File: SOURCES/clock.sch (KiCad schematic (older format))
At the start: 0 parts

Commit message: added clock + extended lib
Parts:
- added C?: 10u, symbol C
- added C?: 100n, symbol C
- added FB?: 330, symbol FILTER
- added U?: 5PB1006CMG, symbol 5PB1006CMG
- added X?: Crystal_Oszillator, symbol Crystal_Oszillator
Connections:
- new net: C?.1, C?.1, FB?.2, U?.12 (VDD), U?.3 (VDD), U?.8 (VDD), X?.1 (Control), X?.4 (Vcc)
- new net: U?.15 (CLKIN), X?.3 (Output)
- new net +3V3: FB?.1
- new net GND: C?.2, C?.2, U?.10 (GND), U?.2 (GND), U?.5 (GND), X?.2 (GND)
- new net MCLK0: U?.1 (Y0)
- new net MCLK1: U?.14 (Y1)
- new net MCLK2: U?.11 (Y2)
- new net MCLK3: U?.13 (Y3)
- new net MCLK4: U?.4 (Y4)
- new net MCLK5: U?.9 (Y5)
- no-connect marks 0 -> 3
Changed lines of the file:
@@
 LIBS:symbols-CS8422-CNZ
 LIBS:symbols_CS8406-CZZ
+LIBS:smd_aio-lib
+LIBS:fdsp_device_new
+LIBS:fdsp_digital_new
+LIBS:fdsp_linear_new
+LIBS:fdsp_oscillator_new
+LIBS:fdsp_transistor_new
 LIBS:smd_aio-cache
 EELAYER 25 0
@@
 $Descr A4 11693 8268
 encoding utf-8
-Sheet 1 7
+Sheet 7 7
 Title ""
 Date ""
@@
 Comment4 ""
 $EndDescr
+$Comp
+L Crystal_Oszillator X?
+U 1 1 5B071476
+P 4510 3290
+F 0 "X?" H 4510 3740 60  0000 C CNN
+F 1 "Crystal_Oszillator" H 4510 2840 60  0000 C CNN
+F 2 "" H 4410 3190 60  0000 C CNN
+F 3 "" H 4410 3190 60  0000 C CNN
+	1    4510 3290
+	1    0    0    -1
+$EndComp
+$Comp
+L FILTER FB?
+U 1 1 5B0715ED
+P 3050 2560
+F 0 "FB?" H 3050 2710 50  0000 C CNN
+F 1 "330" H 3050 2460 50  0000 C CNN
+F 2 "" H 3050 2560 50  0000 C CNN
+F 3 "" H 3050 2560 50  0000 C CNN
+	1    3050 2560
+	0    1    1    0
+$EndComp
+$Comp
+L +3V3 #PWR?
+U 1 1 5B071680
+P 3050 1930
+F 0 "#PWR?" H 3050 1780 50  0001 C CNN
+F 1 "+3V3" H 3050 2070 50  0000 C CNN
+F 2 "" H 3050 1930 60  0000 C CNN
+F 3 "" H 3050 1930 60  0000 C CNN
+	1    3050 1930
+	1    0    0    -1
+$EndComp
+$Comp
+L C C?
+U 1 1 5B0716DF
+P 3050 3270
+F 0 "C?" H 3075 3370 50  0000 L CNN
+F 1 "10u" H 3075 3170 50  0000 L CNN
+F 2 "" H 3088 3120 30  0000 C CNN
+F 3 "" H 3050 3270 60  0000 C CNN
+	1    3050 3270
+	1    0    0    -1
+$EndComp
+$Comp
+L GND #PWR?
+U 1 1 5B071722
+P 3050 3850
+F 0 "#PWR?" H 3050 3600 50  0001 C CNN
+F 1 "GND" H 3050 3700 50  0000 C CNN
+F 2 "" H 3050 3850 60  0000 C CNN
+F 3 "" H 3050 3850 60  0000 C CNN
+	1    3050 3850
+	1    0    0    -1
+$EndComp
+$Comp
+L 5PB1006CMG U?
+U 1 1 5B072592
+P 6950 3730
+F 0 "U?" H 7000 5030 60  0000 C CNN
+F 1 "5PB1006CMG" H 7100 4330 60  0000 C CNN
+F 2 "" H 6950 3730 60  0001 C CNN
+F 3 "" H 6950 3730 60  0001 C CNN
+	1    6950 3730
+	1    0    0    -1
+$EndComp
+Text GLabel 6090 2730 0    60   Output ~ 0
+MCLK0
+Text GLabel 7150 2170 1    60   Output ~ 0
+MCLK1
+Text GLabel 7400 2170 1    60   Output ~ 0
+MCLK3
+Text GLabel 8010 2980 2    60   Output ~ 0
+MCLK2
+Text GLabel 8020 3480 2    60   Output ~ 0
+MCLK5
+NoConn ~ 6650 2280
+$Comp
+L C C?
+U 1 1 5B07311B
+P 5250 3800
+F 0 "C?" H 5275 3900 50  0000 L CNN
+F 1 "100n" H 5275 3700 50  0000 L CNN
+F 2 "" H 5288 3650 30  0000 C CNN
+F 3 "" H 5250 3800 60  0000 C CNN
+	1    5250 3800
+	1    0    0    -1
+$EndComp
+$Comp
+L GND #PWR?
+U 1 1 5B0732C4
+P 5520 4790
+F 0 "#PWR?" H 5520 4540 50  0001 C CNN
+F 1 "GND" H 5520 4640 50  0000 C CNN
+F 2 "" H 5520 4790 60  0000 C CNN
+F 3 "" H 5520 4790 60  0000 C CNN
+	1    5520 4790
+	1    0    0    -1
+$EndComp
+Text GLabel 6100 3480 0    60   Output ~ 0
+MCLK4
+Wire Wire Line
+	5520 2980 6150 2980
+Wire Wire Line
+	6100 3480 6150 3480
+Connection ~ 5250 2730
+Wire Wire Line
+	5250 3650 5250 2730
+Wire Wire Line
+	5440 3540 5060 3540
+Connection ~ 7400 4230
+Wire Wire Line
+	8620 2730 7900 2730
+Wire Wire Line
+	8620 4230 8620 2730
+Connection ~ 5690 3230
+Wire Wire Line
+	7400 4230 7400 3980
+Wire Wire Line
+	5690 4230 8620 4230
+Wire Wire Line
+	5690 3230 6150 3230
+Wire Wire Line
+	5690 2730 5690 4230
+Wire Wire Line
+	3960 2730 5690 2730
+Wire Wire Line
+	5440 2030 6900 2030
+Wire Wire Line
+	6900 2030 6900 2280
+Wire Wire Line
+	7900 3480 8020 3480
+Wire Wire Line
+	7900 2980 8010 2980
+Wire Wire Line
+	7400 2170 7400 2280
+Wire Wire Line
+	7150 2170 7150 2280
+Wire Wire Line
+	6090 2730 6150 2730
+Wire Wire Line
+	5440 2030 5440 3540
+Connection ~ 5060 2730
+Wire Wire Line
+	5060 3040 5060 2730
+Connection ~ 3960 2940
+Connection ~ 3050 3540
+Wire Wire Line
+	3960 3540 3050 3540
+Connection ~ 3050 2940
+Wire Wire Line
+	3960 2730 3960 3040
+Wire Wire Line
+	3050 2940 3960 2940
+Wire Wire Line
+	3050 3420 3050 3850
+Wire Wire Line
+	3050 2910 3050 3120
+Wire Wire Line
+	3050 1930 3050 2210
+Wire Wire Line
+	5520 2980 5520 4790
+Wire Wire Line
+	5250 3950 5250 4490
+Wire Wire Line
+	5250 4490 8840 4490
+Connection ~ 5520 4490
+Wire Wire Line
+	6650 4490 6650 3980
+Wire Wire Line
+	8840 4490 8840 3230
+Wire Wire Line
+	8840 3230 7900 3230
+Connection ~ 6650 4490
+NoConn ~ 6900 3980
+NoConn ~ 7150 3980
 $EndSCHEMATC

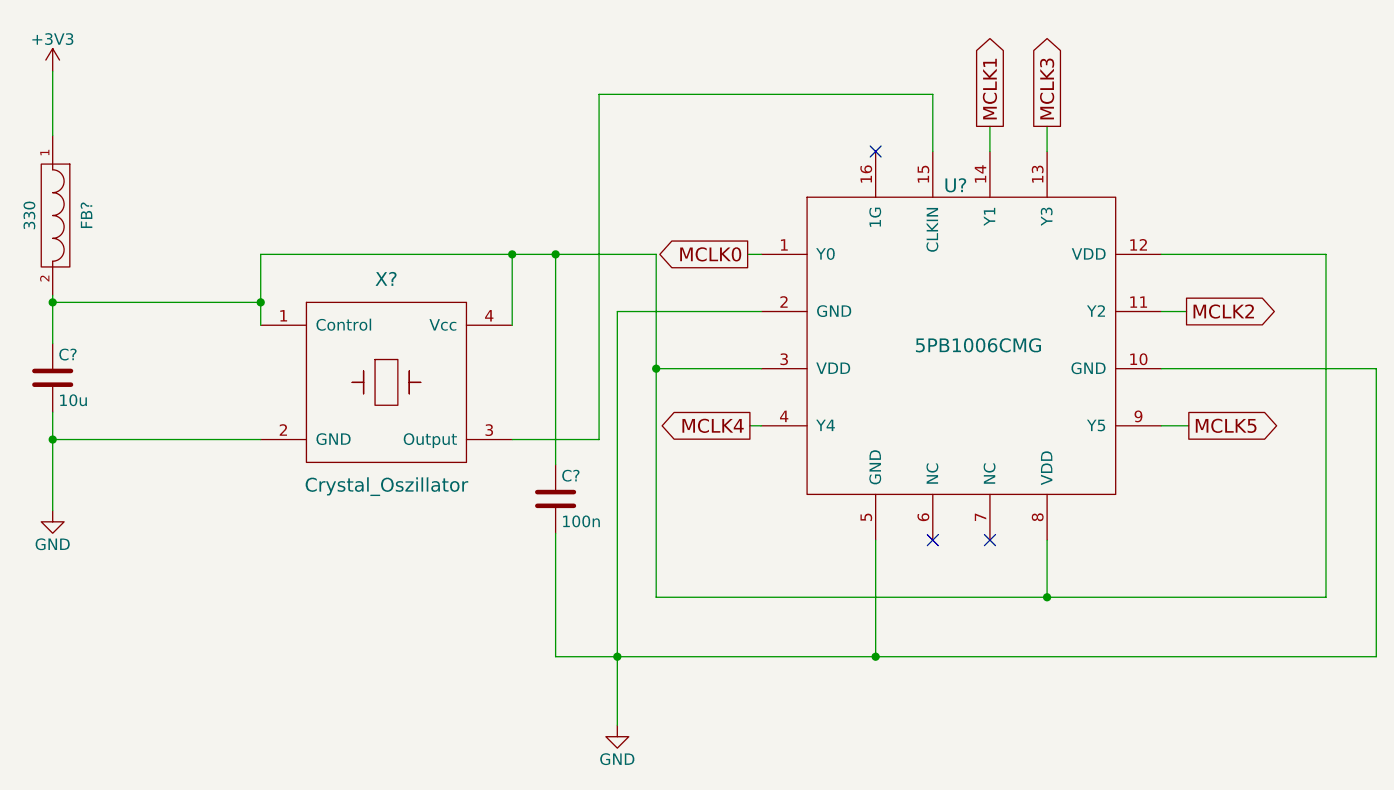
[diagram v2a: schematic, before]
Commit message: added clock
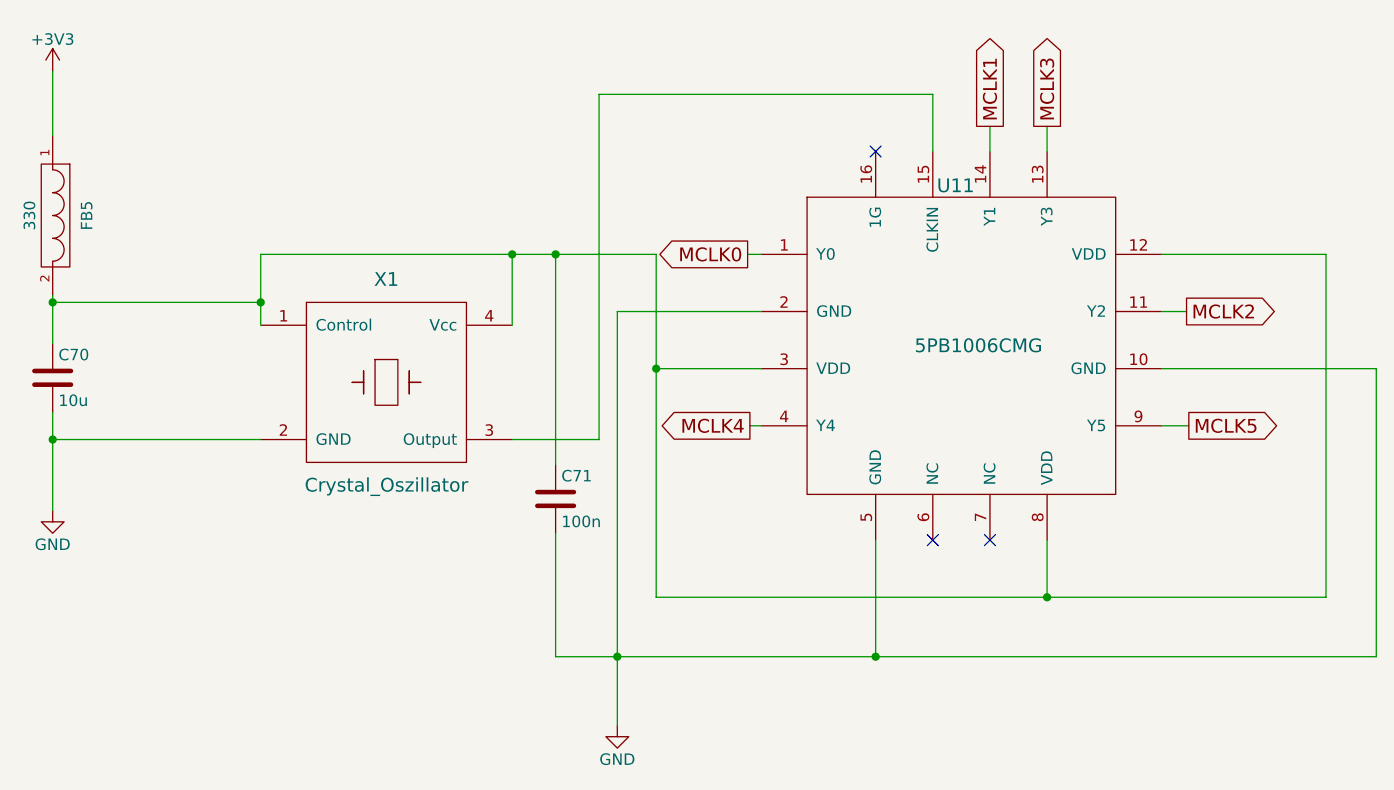
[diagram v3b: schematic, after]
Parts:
- gave numbers to parts that had none: 5
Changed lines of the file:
@@
 $EndDescr
 $Comp
-L Crystal_Oszillator X?
+L Crystal_Oszillator X1
 U 1 1 5B071476
 P 4510 3290
-F 0 "X?" H 4510 3740 60  0000 C CNN
+F 0 "X1" H 4510 3740 60  0000 C CNN
 F 1 "Crystal_Oszillator" H 4510 2840 60  0000 C CNN
 F 2 "" H 4410 3190 60  0000 C CNN
@@
 $EndComp
 $Comp
-L FILTER FB?
+L FILTER FB5
 U 1 1 5B0715ED
 P 3050 2560
-F 0 "FB?" H 3050 2710 50  0000 C CNN
+F 0 "FB5" H 3050 2710 50  0000 C CNN
 F 1 "330" H 3050 2460 50  0000 C CNN
 F 2 "" H 3050 2560 50  0000 C CNN
@@
 $EndComp
 $Comp
-L +3V3 #PWR?
+L +3V3 #PWR109
 U 1 1 5B071680
 P 3050 1930
-F 0 "#PWR?" H 3050 1780 50  0001 C CNN
+F 0 "#PWR109" H 3050 1780 50  0001 C CNN
 F 1 "+3V3" H 3050 2070 50  0000 C CNN
 F 2 "" H 3050 1930 60  0000 C CNN
@@
 $EndComp
 $Comp
-L C C?
+L C C70
 U 1 1 5B0716DF
 P 3050 3270
-F 0 "C?" H 3075 3370 50  0000 L CNN
+F 0 "C70" H 3075 3370 50  0000 L CNN
 F 1 "10u" H 3075 3170 50  0000 L CNN
 F 2 "" H 3088 3120 30  0000 C CNN
@@
 $EndComp
 $Comp
-L GND #PWR?
+L GND #PWR110
 U 1 1 5B071722
 P 3050 3850
-F 0 "#PWR?" H 3050 3600 50  0001 C CNN
+F 0 "#PWR110" H 3050 3600 50  0001 C CNN
 F 1 "GND" H 3050 3700 50  0000 C CNN
 F 2 "" H 3050 3850 60  0000 C CNN
@@
 $EndComp
 $Comp
-L 5PB1006CMG U?
+L 5PB1006CMG U11
 U 1 1 5B072592
 P 6950 3730
-F 0 "U?" H 7000 5030 60  0000 C CNN
+F 0 "U11" H 7000 5030 60  0000 C CNN
 F 1 "5PB1006CMG" H 7100 4330 60  0000 C CNN
 F 2 "" H 6950 3730 60  0001 C CNN
@@
 NoConn ~ 6650 2280
 $Comp
-L C C?
+L C C71
 U 1 1 5B07311B
 P 5250 3800
-F 0 "C?" H 5275 3900 50  0000 L CNN
+F 0 "C71" H 5275 3900 50  0000 L CNN
 F 1 "100n" H 5275 3700 50  0000 L CNN
 F 2 "" H 5288 3650 30  0000 C CNN
@@
 $EndComp
 $Comp
-L GND #PWR?
+L GND #PWR111
 U 1 1 5B0732C4
 P 5520 4790
-F 0 "#PWR?" H 5520 4540 50  0001 C CNN
+F 0 "#PWR111" H 5520 4540 50  0001 C CNN
 F 1 "GND" H 5520 4640 50  0000 C CNN
 F 2 "" H 5520 4790 60  0000 C CNN

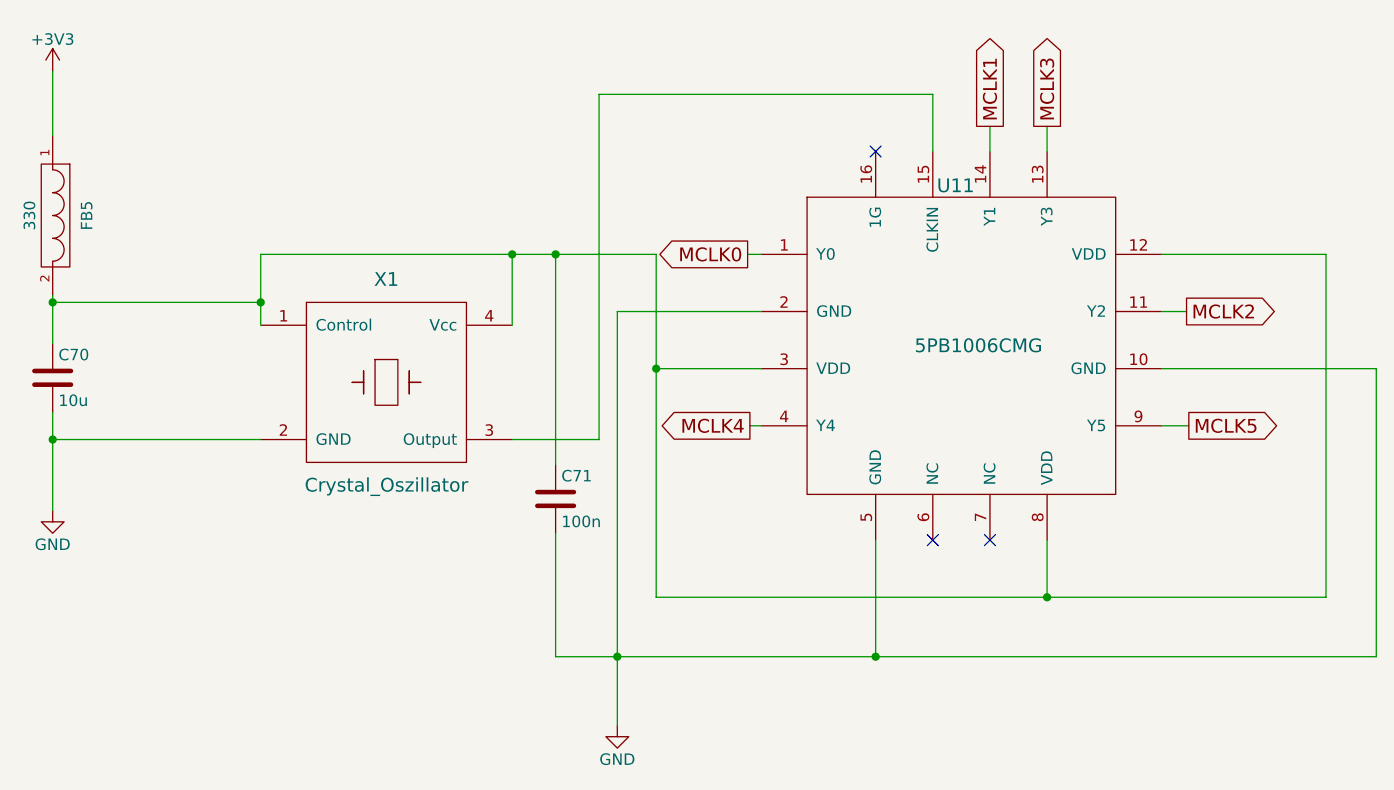
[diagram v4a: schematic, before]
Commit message: IDT2309 clock buffer added
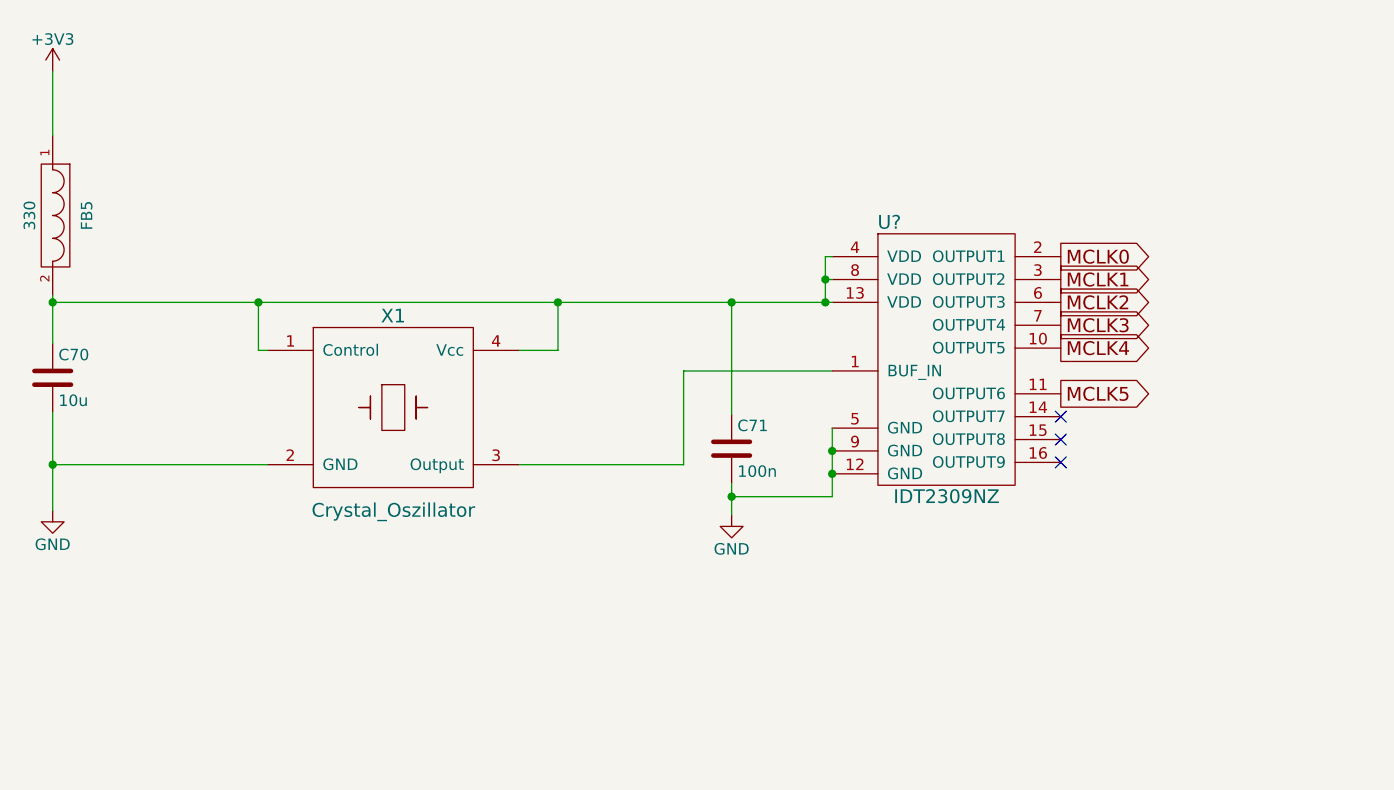
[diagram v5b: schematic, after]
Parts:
- removed U11: 5PB1006CMG, symbol 5PB1006CMG
- added U?: IDT2309NZ, symbol IDT2309NZ
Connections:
- net GND: now also U?.12 (GND), U?.5 (GND), U?.9 (GND)
- net MCLK0: now also U?.2 (OUTPUT1)
- net MCLK1: now also U?.3 (OUTPUT2)
- net MCLK2: now also U?.6 (OUTPUT3)
- net MCLK3: now also U?.7 (OUTPUT4)
- net MCLK4: now also U?.10 (OUTPUT5)
- net MCLK5: now also U?.11 (OUTPUT6)
- net at C70.1, C71.1, FB5.2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: now also U?.13 (VDD), U?.4 (VDD), U?.8 (VDD)
- net at X1.3 (Output): now also U?.1 (BUF_IN)
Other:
- moved on the sheet: C71, X1
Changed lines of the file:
@@
 L Crystal_Oszillator X1
 U 1 1 5B071476
-P 4510 3290
-F 0 "X1" H 4510 3740 60  0000 C CNN
-F 1 "Crystal_Oszillator" H 4510 2840 60  0000 C CNN
-F 2 "" H 4410 3190 60  0000 C CNN
-F 3 "" H 4410 3190 60  0000 C CNN
-	1    4510 3290
+P 4540 3400
+F 0 "X1" H 4540 3800 60  0000 C CNN
+F 1 "Crystal_Oszillator" H 4540 2950 60  0000 C CNN
+F 2 "" H 4440 3300 60  0000 C CNN
+F 3 "" H 4440 3300 60  0000 C CNN
+	1    4540 3400
 	1    0    0    -1
 $EndComp
@@
 	1    0    0    -1
 $EndComp
-$Comp
-L 5PB1006CMG U11
-U 1 1 5B072592
-P 6950 3730
-F 0 "U11" H 7000 5030 60  0000 C CNN
-F 1 "5PB1006CMG" H 7100 4330 60  0000 C CNN
-F 2 "" H 6950 3730 60  0001 C CNN
-F 3 "" H 6950 3730 60  0001 C CNN
-	1    6950 3730
-	1    0    0    -1
-$EndComp
-Text GLabel 6090 2730 0    60   Output ~ 0
+Text GLabel 7460 2740 2    60   Output ~ 0
 MCLK0
-Text GLabel 7150 2170 1    60   Output ~ 0
+Text GLabel 7460 2840 2    60   Output ~ 0
 MCLK1
-Text GLabel 7400 2170 1    60   Output ~ 0
+Text GLabel 7460 3040 2    60   Output ~ 0
 MCLK3
-Text GLabel 8010 2980 2    60   Output ~ 0
+Text GLabel 7460 2940 2    60   Output ~ 0
 MCLK2
-Text GLabel 8020 3480 2    60   Output ~ 0
+Text GLabel 7460 3340 2    60   Output ~ 0
 MCLK5
-NoConn ~ 6650 2280
 $Comp
 L C C71
 U 1 1 5B07311B
-P 5250 3800
-F 0 "C71" H 5275 3900 50  0000 L CNN
-F 1 "100n" H 5275 3700 50  0000 L CNN
-F 2 "" H 5288 3650 30  0000 C CNN
-F 3 "" H 5250 3800 60  0000 C CNN
-	1    5250 3800
+P 6020 3580
+F 0 "C71" H 6045 3680 50  0000 L CNN
+F 1 "100n" H 6045 3480 50  0000 L CNN
+F 2 "" H 6058 3430 30  0000 C CNN
+F 3 "" H 6020 3580 60  0000 C CNN
+	1    6020 3580
 	1    0    0    -1
 $EndComp
@@
 L GND #PWR111
 U 1 1 5B0732C4
-P 5520 4790
-F 0 "#PWR111" H 5520 4540 50  0001 C CNN
-F 1 "GND" H 5520 4640 50  0000 C CNN
-F 2 "" H 5520 4790 60  0000 C CNN
-F 3 "" H 5520 4790 60  0000 C CNN
-	1    5520 4790
+P 6020 3870
+F 0 "#PWR111" H 6020 3620 50  0001 C CNN
+F 1 "GND" H 6020 3720 50  0000 C CNN
+F 2 "" H 6020 3870 60  0000 C CNN
+F 3 "" H 6020 3870 60  0000 C CNN
+	1    6020 3870
 	1    0    0    -1
 $EndComp
-Text GLabel 6100 3480 0    60   Output ~ 0
+Text GLabel 7460 3140 2    60   Output ~ 0
 MCLK4
-Wire Wire Line
-	5520 2980 6150 2980
-Wire Wire Line
-	6100 3480 6150 3480
-Connection ~ 5250 2730
-Wire Wire Line
-	5250 3650 5250 2730
-Wire Wire Line
-	5440 3540 5060 3540
-Connection ~ 7400 4230
-Wire Wire Line
-	8620 2730 7900 2730
-Wire Wire Line
-	8620 4230 8620 2730
-Connection ~ 5690 3230
-Wire Wire Line
-	7400 4230 7400 3980
-Wire Wire Line
-	5690 4230 8620 4230
-Wire Wire Line
-	5690 3230 6150 3230
-Wire Wire Line
-	5690 2730 5690 4230
-Wire Wire Line
-	3960 2730 5690 2730
-Wire Wire Line
-	5440 2030 6900 2030
-Wire Wire Line
-	6900 2030 6900 2280
-Wire Wire Line
-	7900 3480 8020 3480
-Wire Wire Line
-	7900 2980 8010 2980
-Wire Wire Line
-	7400 2170 7400 2280
-Wire Wire Line
-	7150 2170 7150 2280
-Wire Wire Line
-	6090 2730 6150 2730
-Wire Wire Line
-	5440 2030 5440 3540
-Connection ~ 5060 2730
-Wire Wire Line
-	5060 3040 5060 2730
-Connection ~ 3960 2940
-Connection ~ 3050 3540
-Wire Wire Line
-	3960 3540 3050 3540
+$Comp
+L IDT2309NZ U?
+U 1 1 5B108D74
+P 6910 3040
+F 0 "U?" H 6710 3490 60  0000 C CNN
+F 1 "IDT2309NZ" H 6960 2290 60  0000 C CNN
+F 2 "" H 6910 2690 60  0001 C CNN
+F 3 "" H 6910 2690 60  0001 C CNN
+	1    6910 3040
+	1    0    0    -1
+$EndComp
+NoConn ~ 7460 3440
+NoConn ~ 7460 3540
+NoConn ~ 7460 3640
 Connection ~ 3050 2940
-Wire Wire Line
-	3960 2730 3960 3040
-Wire Wire Line
-	3050 2940 3960 2940
 Wire Wire Line
 	3050 3420 3050 3850
@@
 	3050 1930 3050 2210
 Wire Wire Line
-	5520 2980 5520 4790
+	3990 3650 3050 3650
+Connection ~ 3050 3650
 Wire Wire Line
-	5250 3950 5250 4490
+	3950 2940 3950 3150
 Wire Wire Line
-	5250 4490 8840 4490
-Connection ~ 5520 4490
+	3950 3150 3990 3150
+Connection ~ 3950 2940
 Wire Wire Line
-	6650 4490 6650 3980
+	5090 3150 5260 3150
 Wire Wire Line
-	8840 4490 8840 3230
+	5260 3150 5260 2940
+Connection ~ 5260 2940
 Wire Wire Line
-	8840 3230 7900 3230
-Connection ~ 6650 4490
-NoConn ~ 6900 3980
-NoConn ~ 7150 3980
+	5090 3650 5810 3650
+Wire Wire Line
+	5810 3650 5810 3240
+Wire Wire Line
+	5810 3240 6460 3240
+Wire Wire Line
+	6020 3870 6020 3730
+Wire Wire Line
+	6460 3790 6020 3790
+Wire Wire Line
+	6460 3490 6460 3790
+Connection ~ 6020 3790
+Connection ~ 6460 3690
+Connection ~ 6460 3590
+Wire Wire Line
+	3050 2940 6460 2940
+Wire Wire Line
+	6430 2740 6430 2940
+Wire Wire Line
+	6430 2840 6460 2840
+Connection ~ 6430 2940
+Wire Wire Line
+	6430 2740 6460 2740
+Connection ~ 6430 2840
+Wire Wire Line
+	6020 3430 6020 2940
+Connection ~ 6020 2940
 $EndSCHEMATC

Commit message: modifications amp
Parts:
- added R?: 24, symbol R
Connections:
- net MCLK3: now also R?.1; no longer U?.7 (OUTPUT4)
- new net: R?.2, U?.7 (OUTPUT4)
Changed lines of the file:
@@
 Text GLabel 7460 2840 2    60   Output ~ 0
 MCLK1
-Text GLabel 7460 3040 2    60   Output ~ 0
+Text GLabel 8150 3040 2    60   Output ~ 0
 MCLK3
 Text GLabel 7460 2940 2    60   Output ~ 0
@@
 	6020 3430 6020 2940
 Connection ~ 6020 2940
+$Comp
+L R R?
+U 1 1 5B1890A3
+P 7910 3040
+F 0 "R?" V 7990 3040 50  0000 C CNN
+F 1 "24" V 7910 3040 50  0000 C CNN
+F 2 "" V 7840 3040 30  0000 C CNN
+F 3 "" H 7910 3040 30  0000 C CNN
+	1    7910 3040
+	0    1    1    0
+$EndComp
+Wire Wire Line
+	7460 3040 7760 3040
+Wire Wire Line
+	8060 3040 8150 3040
 $EndSCHEMATC
